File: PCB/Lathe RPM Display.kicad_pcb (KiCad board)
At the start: 2 copper layers, 18 parts, among them Q1 OH090U, Q2 2N7000, Q3 2N7000, Q4 2N7000, Q5 2N7000, U1 KCSC02-105, U2 KCSC02-105, U3 KCSC02-105, U4 KCSC02-105

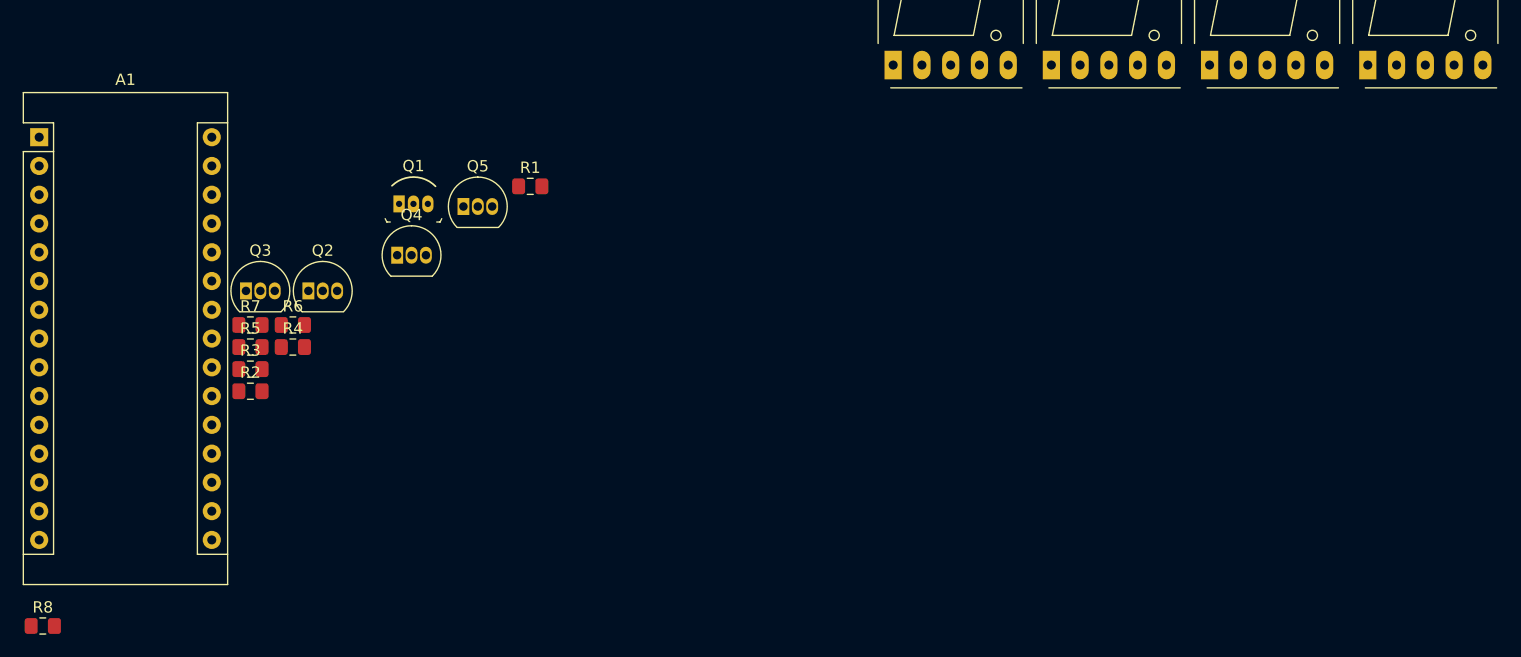
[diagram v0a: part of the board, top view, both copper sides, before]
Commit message: code, schematic and layout
Got code to a good working state. Schematic is good, maybe a couple more additions for power. Started layout and happy with locations. No traces routed.
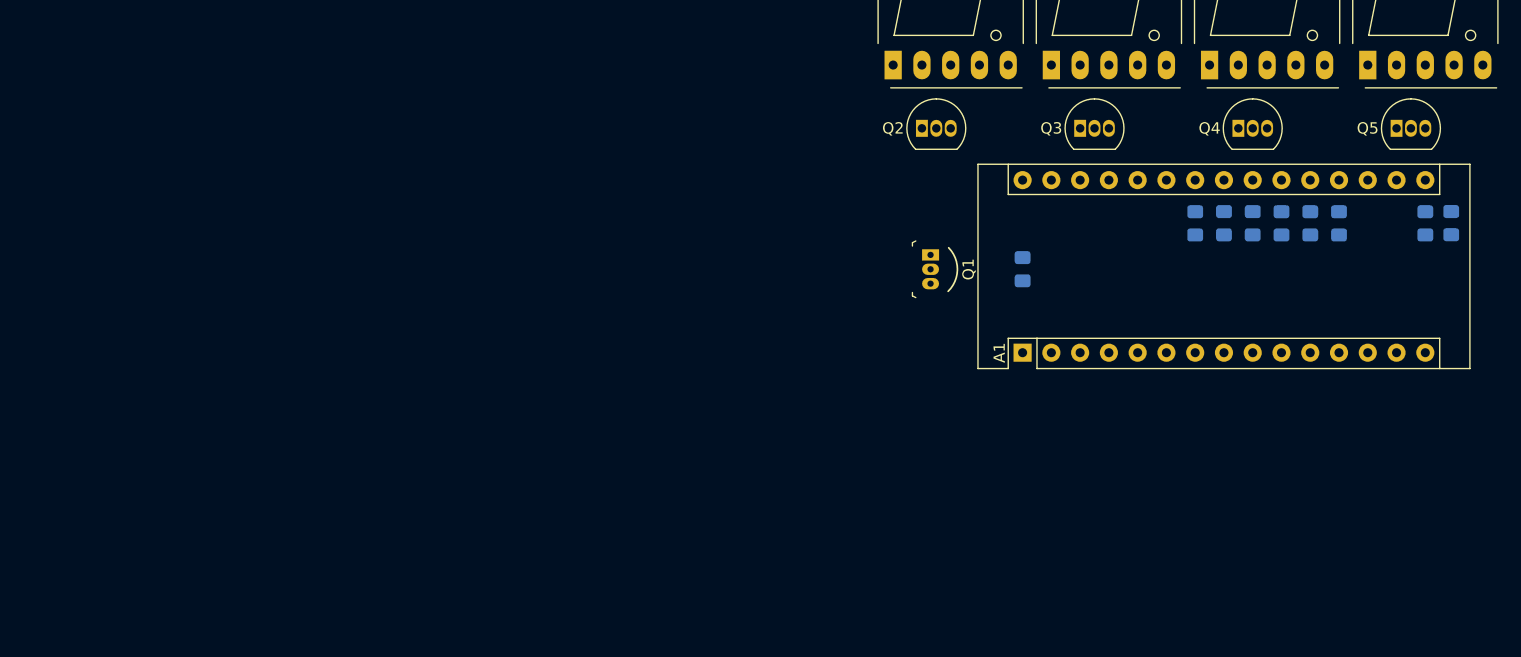
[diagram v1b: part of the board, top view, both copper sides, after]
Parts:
- added R9: 10k, Resistor_SMD:R_0805_2012Metric_Pad1.15x1.40mm_HandSolder, B.Cu at (168.9, 86.6)
- Q1: value OH090U -> A3144EU
- R1, R2, R3, R4, R5, R6, R7, R8: moved to B.Cu
- moved R8 129.3 mm to (206.8, 82.5), turned to 270 degrees
- moved R7 104.1 mm to (204.5, 82.6), turned to 90 degrees
- moved R2 94.8 mm to (194.3, 82.6), turned to 90 degrees
- moved R3 92.0 mm to (191.8, 82.6), turned to 90 degrees
- moved A1 88.9 mm to (168.9, 94.0), turned to 90 degrees
- moved R5 86.7 mm to (186.7, 82.5), turned to 90 degrees
- moved R4 85.5 mm to (189.2, 82.5), turned to 90 degrees
- moved Q5 82.7 mm to (201.9, 74.2)
- moved R6 80.2 mm to (184.2, 82.6), turned to 90 degrees
- moved Q4 75.1 mm to (188.0, 74.2)
- moved Q3 75.0 mm to (174.0, 74.2)
- moved R1 71.5 mm to (196.8, 82.6), turned to 90 degrees
- moved Q2 56.0 mm to (160.0, 74.2)
- moved Q1 47.1 mm to (160.8, 85.3), turned to 270 degrees
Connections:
- A1 pad 15: (no net) -> /DP
- A1 pad 16: (no net) -> /G
- A1 pad 25: /G -> (no net)
- A1 pad 26: /DP -> (no net)

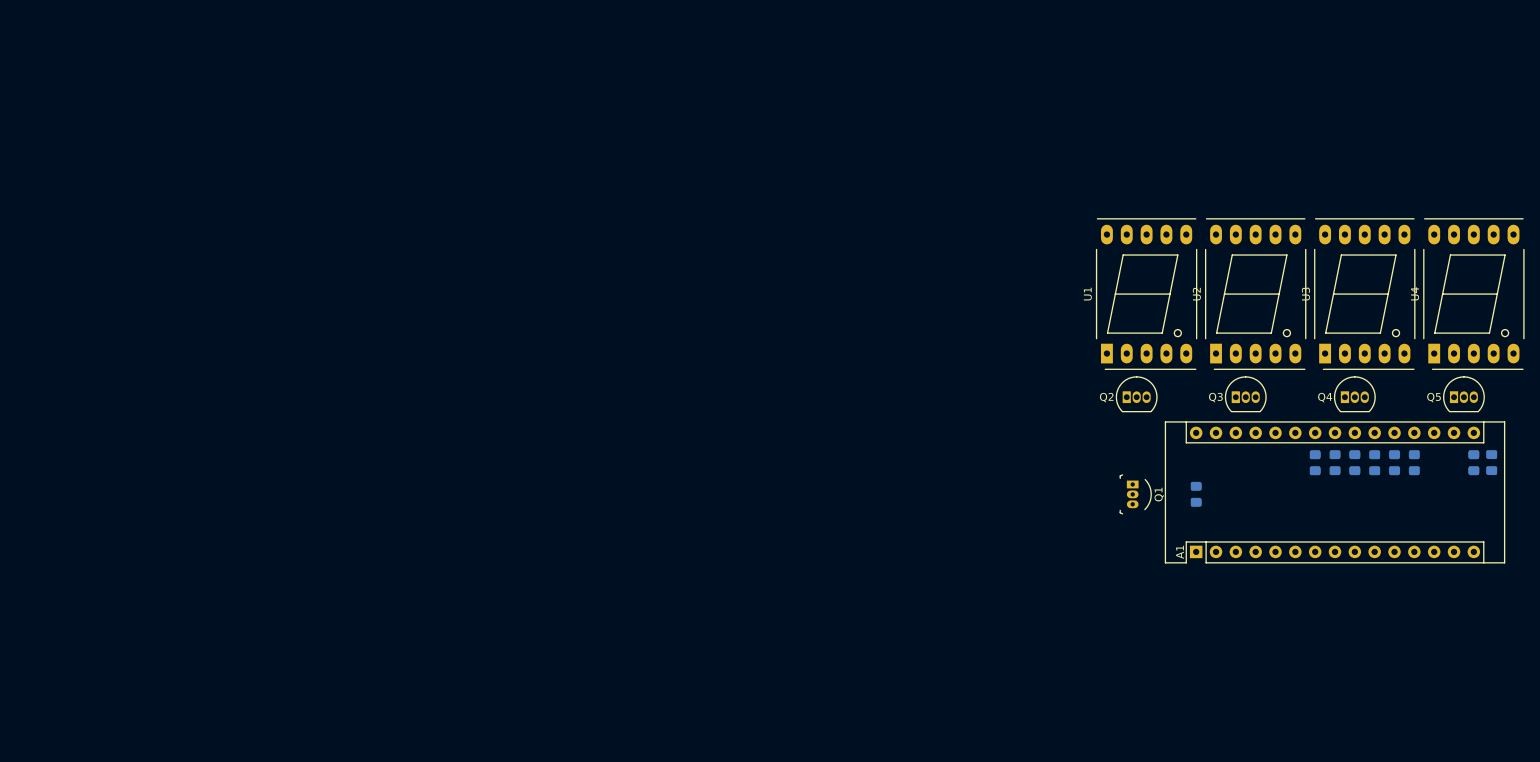
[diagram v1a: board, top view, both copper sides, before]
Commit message: hall effect fix
Adjusted pulses per revolution to fix hall effect sensor double pulse
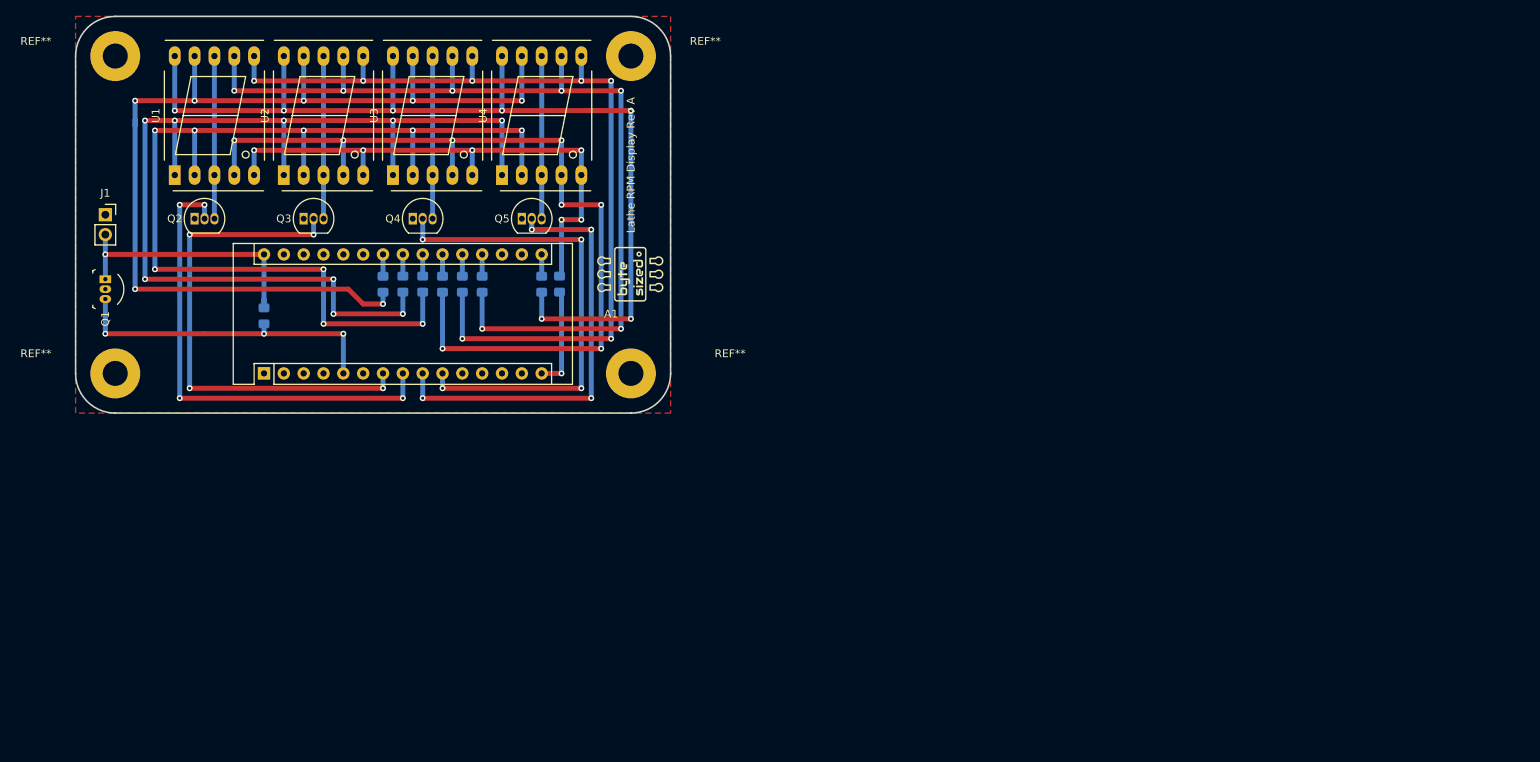
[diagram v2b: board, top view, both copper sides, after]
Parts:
- added G***: LOGO, User_Footprint:byte_sized_logo_stroke-10x10mm, F.Cu at (96.5, 58.4)
- added J1: Conn_01x02, Connector_PinSocket_2.54mm:PinSocket_1x02_P2.54mm_Vertical, F.Cu at (29.2, 50.8)
- added REF**: MountingHole_3.2mm_M3_Pad, MountingHole:MountingHole_3.2mm_M3_Pad, F.Cu at (96.5, 30.5)
- added REF**: MountingHole_3.2mm_M3_Pad, MountingHole:MountingHole_3.2mm_M3_Pad, F.Cu at (96.5, 71.1)
- added REF**: MountingHole_3.2mm_M3_Pad, MountingHole:MountingHole_3.2mm_M3_Pad, F.Cu at (30.5, 71.1)
- added REF**: MountingHole_3.2mm_M3_Pad, MountingHole:MountingHole_3.2mm_M3_Pad, F.Cu at (30.5, 30.5)
- moved Q1 134.2 mm to (29.2, 59.1)
- moved Q2 121.5 mm to (40.6, 51.3)
- moved Q3 121.5 mm to (54.6, 51.3)
- moved Q4 121.5 mm to (68.6, 51.3)
- moved Q5 121.5 mm to (82.5, 51.3)
- moved R3 121.5 mm to (72.4, 59.7)
- moved R6 121.5 mm to (64.8, 59.7)
- moved A1 121.5 mm to (49.5, 71.1)
- moved R1 121.5 mm to (77.5, 59.7)
- moved R2 121.5 mm to (74.9, 59.7)
- moved R4 121.5 mm to (69.8, 59.7)
- moved R5 121.5 mm to (67.3, 59.7)
- moved R7 121.5 mm to (85.1, 59.7)
- moved R8 121.5 mm to (87.4, 59.7)
- moved R9 121.5 mm to (49.5, 63.7)
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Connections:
- Q2 pad 2: Net-(A1-Pad10) -> Net-(A1-Pad8)
- Q3 pad 2: Net-(A1-Pad9) -> Net-(A1-Pad7)
- Q4 pad 2: Net-(A1-Pad8) -> Net-(A1-Pad10)
- Q5 pad 2: Net-(A1-Pad7) -> Net-(A1-Pad9)
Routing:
- net Net-(R5-Pad1): track 0.00 -> 134.2 mm, vias 0 -> 9
- net Net-(R4-Pad1): track 0.00 -> 133.0 mm, vias 0 -> 9
- net Net-(R6-Pad1): track 0.00 -> 131.8 mm, vias 0 -> 7
- net Net-(R7-Pad1): track 0.00 -> 129.8 mm, vias 0 -> 7
- net Net-(R1-Pad1): track 0.00 -> 120.3 mm, vias 0 -> 7
- net Net-(R2-Pad1): track 0.00 -> 116.4 mm, vias 0 -> 7
- net Net-(R3-Pad1): track 0.00 -> 114.5 mm, vias 0 -> 8
- net Net-(R8-Pad1): track 0.00 -> 70.2 mm, vias 0 -> 6
- net Net-(A1-Pad7): track 0.00 -> 64.3 mm, vias 0 -> 4
- net Net-(A1-Pad10): track 0.00 -> 61.7 mm, vias 0 -> 4
- net Net-(A1-Pad8): track 0.00 -> 61.5 mm, vias 0 -> 4
- net Net-(A1-Pad9): track 0.00 -> 55.4 mm, vias 0 -> 4
- net Net-(A1-Pad5): track 0.00 -> 41.3 mm, vias 0 -> 3
- net +5V: track 0.00 -> 34.0 mm, vias 0 -> 1
- net Net-(Q5-Pad3): track 0.00 -> 20.8 mm
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- added copper zone on F.Cu, net GND
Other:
- board outline added: 76.2 x 50.8 mm
- rule trace_min: 0.2 -> 0.0889
- rule via_min_drill: 0.3 -> 0.2032
- rule via_min_size: 0.4 -> 0.4572
- board text added: "Lathe RPM Display Rev A"
